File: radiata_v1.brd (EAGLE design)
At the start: 80 x 80 mm, 91 parts, among them IC1 TINY24/44/84-SSU, IC2 MEGA48/88/168-AU

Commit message: rename simpleclock to 'radiata'
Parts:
- removed IC1: TINY24/44/84-SSU, avr-7:SOIC14
- removed RDOWN, RUP: (no value), SparkFun:1206
- added C1, C2: (no value), rcl:C0603
- added DOWNSW, UPSW: SWITCH-MOMENTARY-2, SparkFun:TACTILE_SWITCH_TALL
- added Q1: FA-20H, crystal:FA-20H
- moved IC2 57.7 mm to (40.0, 40.0), turned to 45 degrees
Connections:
- removed net AGND: IC2.21
- removed net PA0: IC1.13, RN1.1
- removed net PA1: IC1.12, RN2.1
- removed net PA2: IC1.11, RN3.1
- removed net PA3: IC1.10, RN4.1
- removed net PA4: IC1.9, RN5.1, SCL.TP
- removed net PA5: IC1.8, MISO.TP, RN6.1
- removed net PA6: IC1.7, MOSI.TP, RN7.1
- removed net PA7: IC1.6, RN8.1
- removed net PB2: IC1.5, RN9.1
- removed net PB3: IC1.4, RDOWN.1, RESET.TP, RUP.1
- new net N$5: IC2.29, RESET.TP
- new net N$6: IC2.17, SCL.TP
- new net N$7: IC2.16, MISO.TP
- new net N$8: IC2.15, MOSI.TP
- new net PC0: IC2.23, RN9.1
- new net PC1: IC2.24, UPSW.A2
- new net PC2: DOWNSW.A2, IC2.25
- new net PC3: IC2.26
- new net PC4: IC2.27
- new net PC5: IC2.28
- new net PD0: IC2.30, RN1.1
- new net PD1: IC2.31, RN2.1
- new net PD2: IC2.32, RN3.1
- new net PD3: IC2.1, RN4.1
- new net PD4: IC2.2, RN5.1
- new net PD5: IC2.9, RN6.1
- new net PD6: IC2.10, RN7.1
- new net PD7: IC2.11, RN8.1
- net GND: now also C1.2, C2.2, DOWNSW.B2, IC2.21, UPSW.B2; no longer IC1.14
- net PB0: now also C2.1, IC2.8, Q1.3; no longer IC1.2, RUP.2
- net PB1: now also C1.1, IC2.7, Q1.1; no longer IC1.3, RDOWN.2
- net VCC: now also IC2.18; no longer IC1.1
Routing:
- net PA0: track 30.4 -> 0.00 mm
- net PA1: track 13.4 -> 0.00 mm
- net PA2: track 12.2 -> 0.00 mm
- net PB3: track 11.7 -> 0.00 mm
- net PA4: track 11.3 -> 0.00 mm
- net PA3: track 10.8 -> 0.00 mm
- net PA7: track 9.19 -> 0.00 mm
- net PB2: track 8.86 -> 0.00 mm
- net PA6: track 8.55 -> 0.00 mm
- net PA5: track 8.04 -> 0.00 mm
- net PB1: track 6.02 -> 0.00 mm, vias 1 -> 0
- net GND: track 3.70 -> 0.00 mm
- net VCC: track 3.70 -> 0.00 mm
- net PB0: track 1.97 -> 0.00 mm, vias 1 -> 0
- removed copper zone on layer 16, net PB0
- removed copper zone on layer 16, net PB1

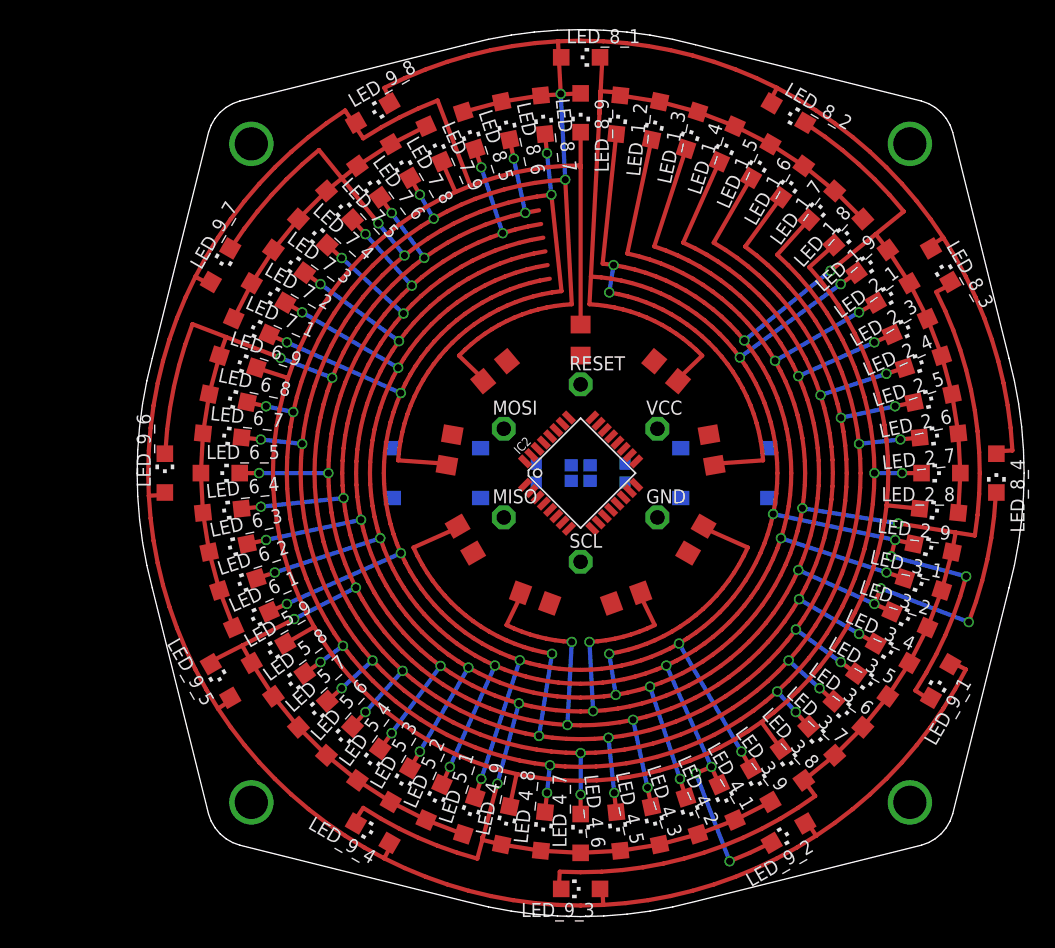
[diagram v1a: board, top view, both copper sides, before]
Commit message: fix a routing issue; adjust scroll rotor size
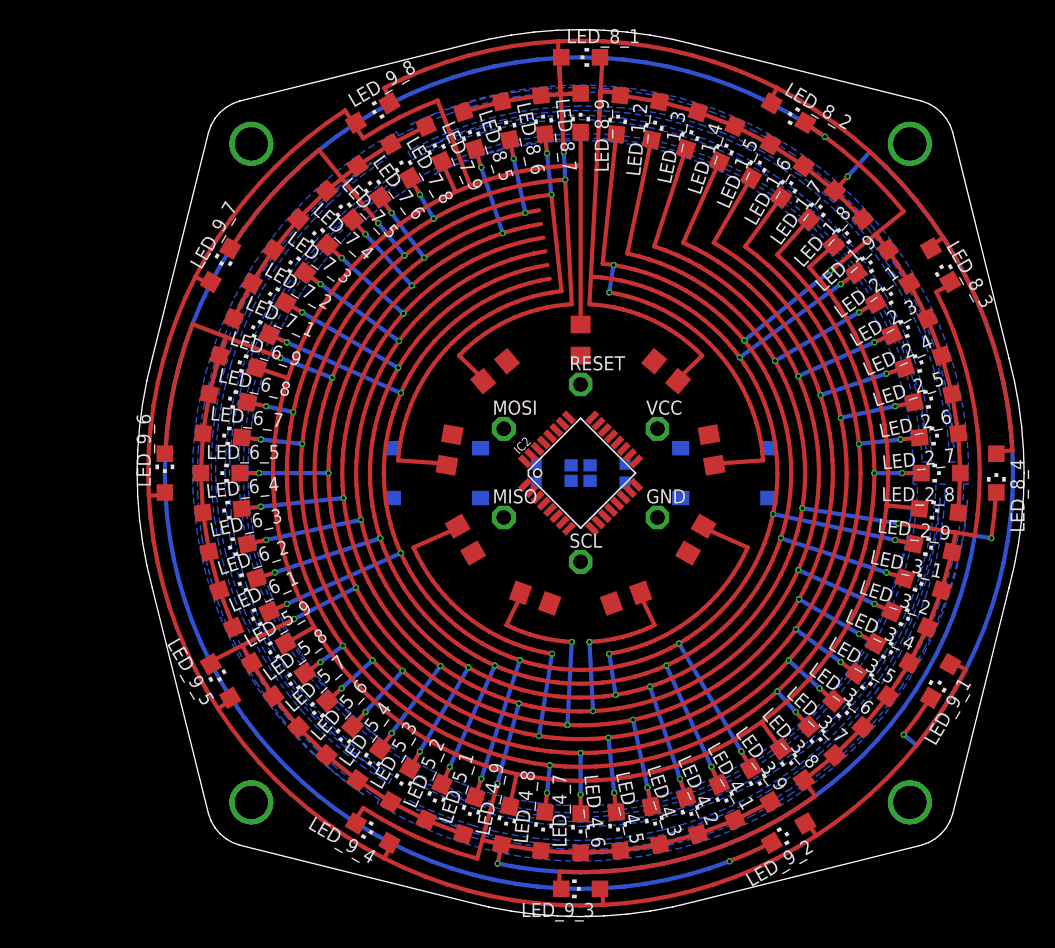
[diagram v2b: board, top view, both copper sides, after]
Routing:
- net N_2: track 285.8 -> 429.8 mm
- net N_1: track 273.9 -> 320.3 mm
- net N_4: track 272.8 -> 315.1 mm
- net N_9: track 363.7 -> 361.6 mm
- net N_3: track 302.6 -> 301.5 mm
- net N_7: track 264.4 -> 263.5 mm
- net N_5: track 244.7 -> 243.8 mm
- net N_6: track 262.6 -> 261.8 mm
- added copper zone on layer 16, net N$10
- added copper zone on layer 16, net N$11
- added copper zone on layer 16, net N$9

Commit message: lots of progress, driving towards a scroll wheel that passes DRC
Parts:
- added GND2, V+: PTR1TP20SQ, testpad:TP20SQ
- added RR1, RR2, RR3, RS1, RS2, RS3: (no value), SparkFun:1206
- moved DOWNSW 6.73 mm to (28.7, 46.5), turned to 120 degrees
- moved UPSW 6.73 mm to (51.3, 46.5), turned to 240 degrees
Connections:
- new net ROTOR1: RR1.1, RS1.2
- new net ROTOR2: RR2.1, RS2.2
- new net ROTOR3: RR3.1, RS3.2
- net GND: now also GND2.TP
- net PC2: now also RS1.1, RS2.1, RS3.1
- net PC3: now also RR1.2
- net PC4: now also RR2.2
- net PC5: now also RR3.2
- net VCC: now also V+.TP
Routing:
- net PC2: track 0.00 -> 68.3 mm, vias 0 -> 2
- net GND: track 0.00 -> 56.7 mm, vias 0 -> 4
- net VCC: track 0.00 -> 33.3 mm, vias 0 -> 2
- net PD7: track 0.00 -> 32.9 mm, vias 0 -> 2
- net N$8: track 0.00 -> 32.6 mm, vias 0 -> 2
- net PC5: track 0.00 -> 30.4 mm, vias 0 -> 1
- net PD1: track 0.00 -> 28.8 mm, vias 0 -> 2
- net PD6: track 0.00 -> 27.0 mm, vias 0 -> 2
- net PC1: track 0.00 -> 23.9 mm, vias 0 -> 1
- net PD2: track 0.00 -> 23.2 mm, vias 0 -> 2
- net ROTOR1: track 0.00 -> 20.0 mm
- net ROTOR2: track 0.00 -> 20.0 mm
- net ROTOR3: track 0.00 -> 19.8 mm
- net PC4: track 0.00 -> 16.9 mm, vias 0 -> 1
- net PD3: track 0.00 -> 15.7 mm
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- added copper zone on layer 16, net ROTOR1
- added copper zone on layer 16, net ROTOR2
- added copper zone on layer 16, net ROTOR3
- removed copper zone on layer 16, net N$10
- removed copper zone on layer 16, net N$11
- removed copper zone on layer 16, net N$9

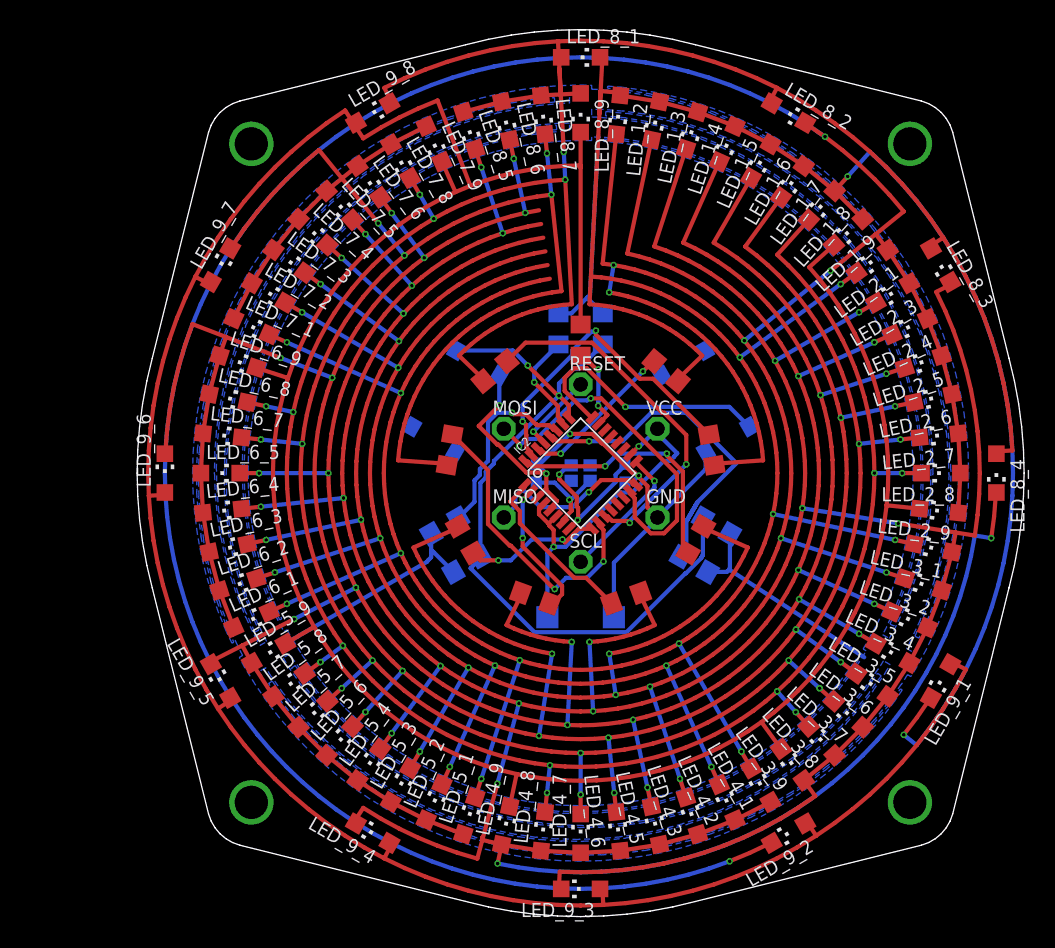
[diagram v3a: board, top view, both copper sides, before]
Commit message: add push/pull resistors
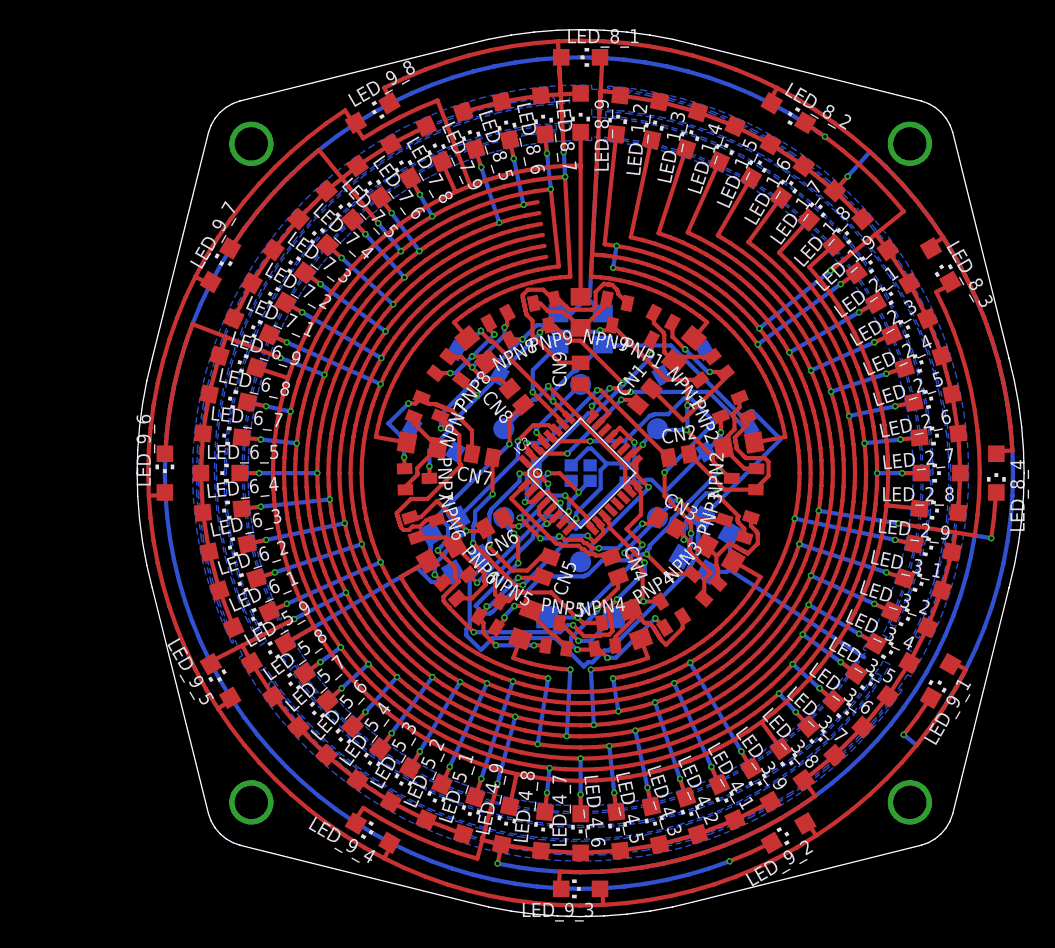
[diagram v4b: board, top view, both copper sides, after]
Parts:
- added CN1, CN2, CN3, CN4, CN5, CN6, CN7, CN8, CN9: (no value), rcl:M0805
- added NPN1, NPN2, NPN3, NPN4, NPN5, NPN6, NPN7, NPN8, NPN9, PNP1, PNP2, PNP3, PNP4, PNP5, PNP6, PNP7, PNP8, PNP9: (no value), transistor:SOT23-BEC
- GND, MISO, MOSI, RESET, SCL, VCC: value PTR1PAD1-13 -> PTR1TP19R; device testpad:P1-13 -> testpad:TP19R
- moved RN1 2.50 mm to (49.3, 51.1), turned to 50 degrees
- moved RN8 2.50 mm to (30.7, 51.1), turned to 130 degrees
- moved RN9 2.50 mm to (40.0, 54.5)
- moved RN2 2.50 mm to (54.3, 42.5), turned to 10 degrees
- moved RN7 2.50 mm to (25.7, 42.5), turned to 170 degrees
- moved RN4 2.50 mm to (45.0, 26.4), turned to 290 degrees
- moved RN5 2.50 mm to (35.0, 26.4), turned to 250 degrees
- moved RN3 2.50 mm to (52.6, 32.8), turned to 330 degrees
- moved RN6 2.50 mm to (27.4, 32.8), turned to 210 degrees
- flipped GND to the bottom
- flipped MISO to the bottom
- flipped MOSI to the bottom
- flipped RESET to the bottom
- flipped SCL to the bottom
- flipped VCC to the bottom
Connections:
- new net N$10: CN1.2, NPN1.B, PNP1.B
- new net N$11: NPN2.E, PNP2.E, RN2.1
- new net N$12: CN2.2, NPN2.B, PNP2.B
- new net N$13: NPN3.E, PNP3.E, RN3.1
- new net N$14: CN3.2, NPN3.B, PNP3.B
- new net N$15: NPN4.E, PNP4.E, RN4.1
- new net N$16: CN4.2, NPN4.B, PNP4.B
- new net N$17: NPN5.E, PNP5.E, RN5.1
- new net N$18: CN5.2, NPN5.B, PNP5.B
- new net N$19: NPN6.E, PNP6.E, RN6.1
- new net N$20: CN6.2, NPN6.B, PNP6.B
- new net N$24: NPN7.E, PNP7.E, RN7.1
- new net N$25: CN7.2, NPN7.B, PNP7.B
- new net N$26: NPN8.E, PNP8.E, RN8.1
- new net N$27: CN8.2, NPN8.B, PNP8.B
- new net N$28: NPN9.E, PNP9.E, RN9.1
- new net N$29: CN9.2, NPN9.B, PNP9.B
- new net N$9: NPN1.E, PNP1.E, RN1.1
- net GND: now also PNP1.C, PNP2.C, PNP3.C, PNP4.C, PNP5.C, PNP6.C, PNP7.C, PNP8.C, PNP9.C
- net PC0: now also CN9.1; no longer RN9.1
- net PD0: now also CN1.1; no longer RN1.1
- net PD1: now also CN2.1; no longer RN2.1
- net PD2: now also CN3.1; no longer RN3.1
- net PD3: now also CN4.1; no longer RN4.1
- net PD4: now also CN5.1; no longer RN5.1
- net PD5: now also CN6.1; no longer RN6.1
- net PD6: now also CN7.1; no longer RN7.1
- net PD7: now also CN8.1; no longer RN8.1
- net VCC: now also NPN1.C, NPN2.C, NPN3.C, NPN4.C, NPN5.C, NPN6.C, NPN7.C, NPN8.C, NPN9.C
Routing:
- net VCC: track 33.3 -> 118.5 mm, vias 2 -> 11
- net GND: track 56.7 -> 123.6 mm, vias 4 -> 14
- net N$29: track 0.00 -> 22.4 mm
- net PC2: track 68.3 -> 89.8 mm
- net PD7: track 32.9 -> 53.8 mm, vias 2 -> 6
- net N$7: track 15.3 -> 35.0 mm, vias 1 -> 3
- net N$14: track 0.00 -> 19.1 mm, vias 0 -> 2
- net N$16: track 0.00 -> 18.7 mm, vias 0 -> 4
- net N$10: track 0.00 -> 17.4 mm, vias 0 -> 2
- net N$12: track 0.00 -> 17.1 mm
- net N$25: track 0.00 -> 16.5 mm, vias 0 -> 2
- net N$18: track 0.00 -> 15.2 mm, vias 0 -> 4
- net N$20: track 0.00 -> 14.8 mm, vias 0 -> 2
- net N$8: track 32.6 -> 18.2 mm, vias 2 -> 1
- net N$27: track 0.00 -> 13.0 mm, vias 0 -> 2
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
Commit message: final versions of board and schematic
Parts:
- removed SCL: PTR1TP19R, testpad:TP19R
- added C3: (no value), rcl:C0603
- added SCK: PTR1TP19R, testpad:TP19R
- moved GND 16.0 mm to (33.1, 44.0)
- moved VCC 16.0 mm to (33.1, 36.0)
- moved MOSI 13.9 mm to (40.0, 32.0)
- moved MISO 13.9 mm to (46.9, 36.0)
- moved C1 2.07 mm to (36.5, 38.0), turned to 60 degrees
- moved C2 2.07 mm to (43.5, 38.0), turned to 300 degrees
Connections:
- net GND: now also C3.2
- net N$6: now also SCK.TP; no longer SCL.TP
- net VCC: now also C3.1
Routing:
- net PC2: track 89.8 -> 57.7 mm, vias 2 -> 5
- net N$7: track 35.0 -> 3.76 mm, vias 3 -> 1
- net PD6: track 25.3 -> 52.8 mm
- net N$8: track 18.2 -> 8.58 mm
- net PD4: track 18.0 -> 9.31 mm
- net N$6: track 12.1 -> 3.80 mm
- net PC5: track 32.9 -> 40.7 mm, vias 3 -> 1
- net N$29: track 22.4 -> 29.4 mm
- net PD7: track 53.8 -> 47.0 mm, vias 6 -> 2
- net N$14: track 19.1 -> 13.7 mm, vias 2 -> 0
- net N$28: track 8.84 -> 13.6 mm, vias 0 -> 2
- net PD1: track 18.6 -> 13.9 mm
- net N$10: track 17.4 -> 12.9 mm, vias 2 -> 3
- net N$20: track 14.8 -> 18.3 mm
- net PC1: track 17.5 -> 20.9 mm, vias 3 -> 5
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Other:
- board text added: "-"
- board text added: "0"
- board text added: "1"
- board text added: "2"
- board text added: "3"
- board text added: "9"
- board text added: "a"
- board text added: "b"
- board text added: "d"
- board text added: "i"
- board text added: "n"
- board text added: "r"
- board text added: "t"
- board text added: "u"
- board text added: "v"
- board text added: "x"
- board text added: "y"
